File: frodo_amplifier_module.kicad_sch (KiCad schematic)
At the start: 24 parts, among them IC1 INA826AID, U1 NCS20071SN

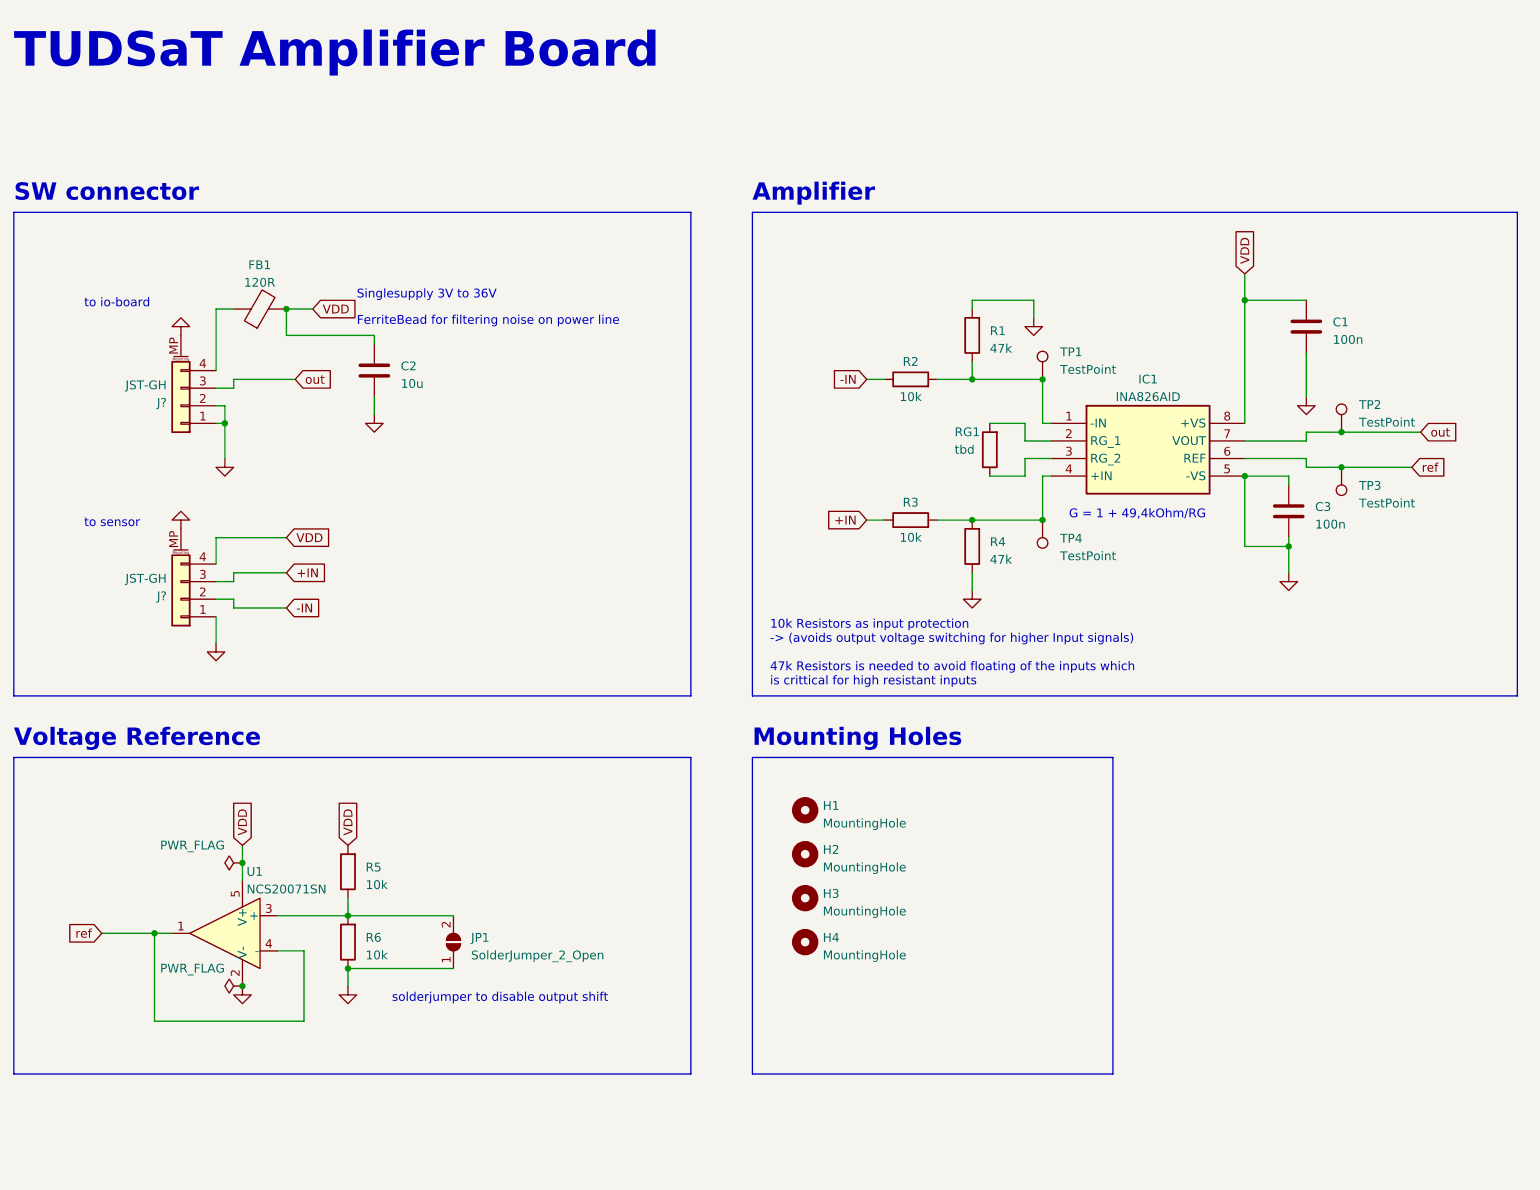
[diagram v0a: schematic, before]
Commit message: updated amplifier module, removed mounting holes and routed the pcb
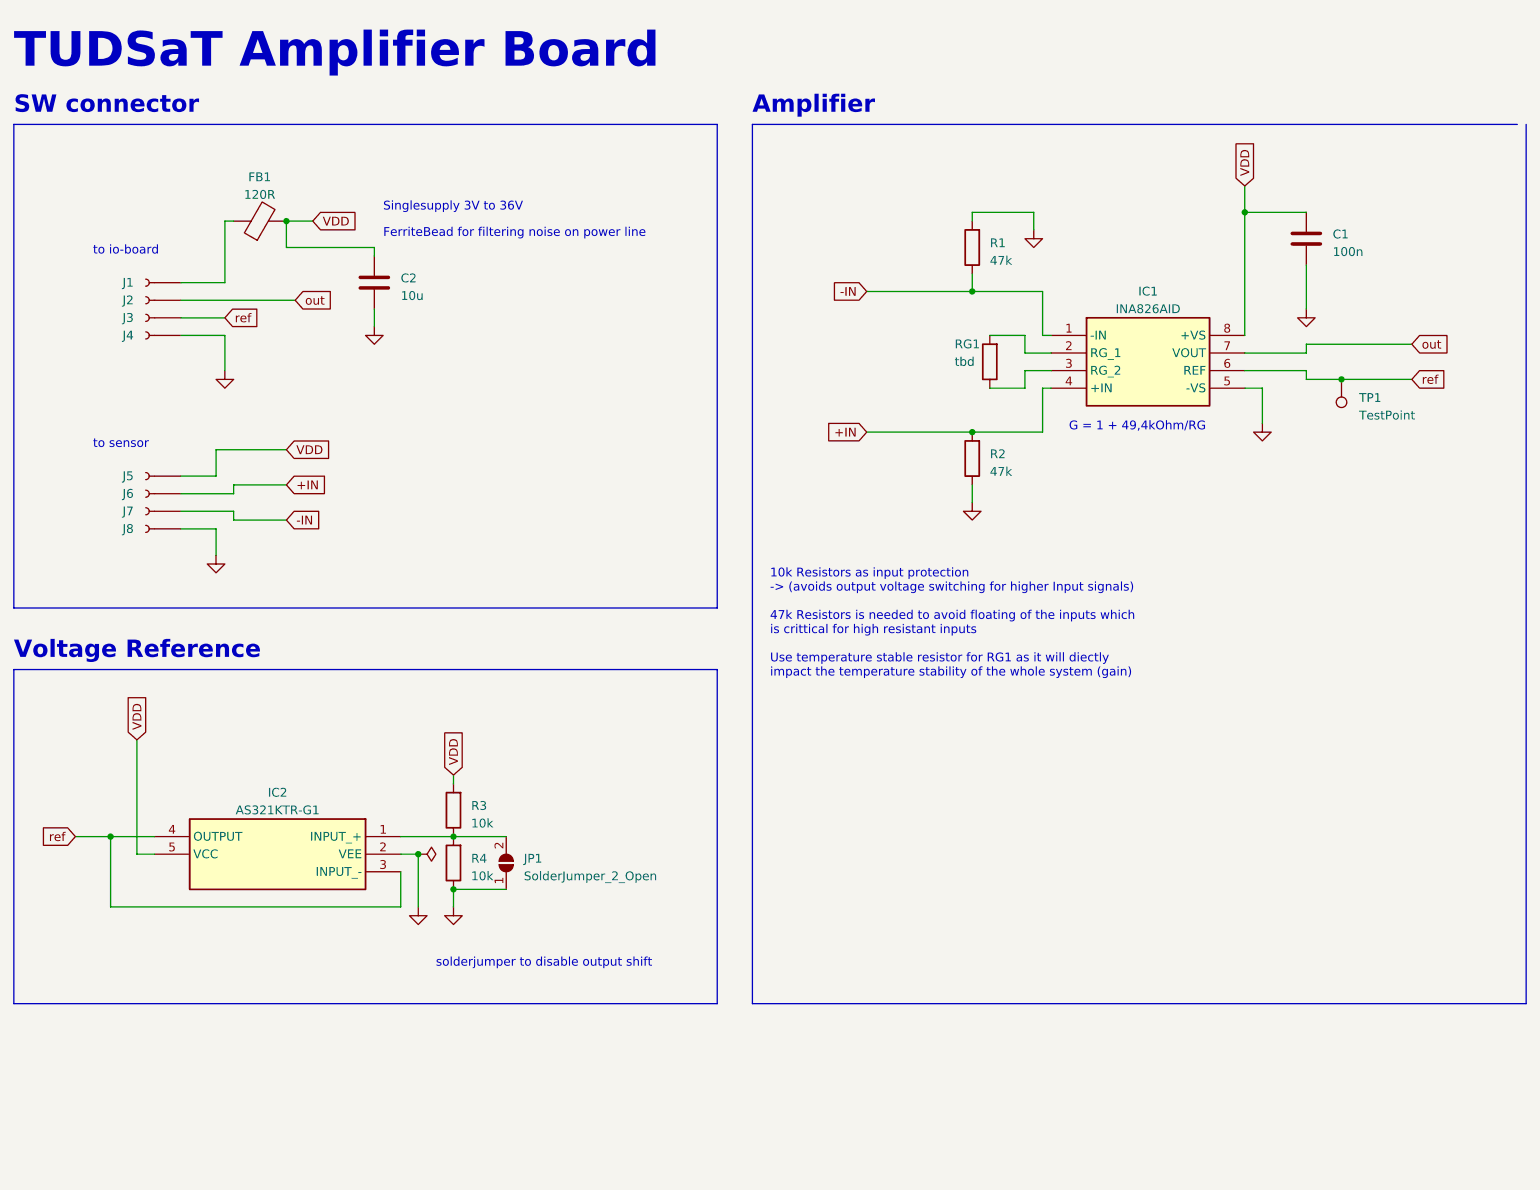
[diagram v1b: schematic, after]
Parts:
- removed C3: 100n, Capacitor_SMD:C_0402_1005Metric_Pad0.74x0.62mm_HandSolder, symbol Device:C
- removed H1, H2, H3, H4: MountingHole, MountingHole:MountingHole_2.2mm_M2_ISO7380_Pad, symbol Mechanical:MountingHole
- removed J? (x2): JST-GH, Connector_JST:JST_GH_SM04B-GHS-TB_1x04-1MP_P1.25mm_Horizontal, symbol Connector_Generic_MountingPin:Conn_01x04_MountingPin
- removed R2, R3: 10k, Resistor_SMD:R_0402_1005Metric_Pad0.72x0.64mm_HandSolder, symbol Device:R
- removed TP1, TP2, TP4: TestPoint, TestPoint:TestPoint_Pad_D1.5mm, symbol Connector:TestPoint
- removed U1: NCS20071SN, Package_SO:TSOP-5_1.65x3.05mm_P0.95mm, symbol Amplifier_Operational:NCS20071SN
- added IC2: AS321KTR-G1, Package_TO_SOT_SMD:SOT-23-5, symbol AS321KTR-G1:AS321KTR-G1
- added J1, J2, J3, J4, J5, J6, J7, J8: Conn_01x01_Socket, Connector_Wire:SolderWirePad_1x01_SMD_1x2mm, symbol Connector:Conn_01x01_Socket
- renumbered R4 to R2, R5 to R3, R6 to R4, TP3 to TP1
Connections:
- net +IN: now also IC1.4 (+IN), R2.2, J6.1 (Pin_1)
- net -IN: now also IC1.1 (-IN), R1.1, J7.1 (Pin_1)
- net GND: now also IC2.2 (VEE), J4.1 (Pin_1), J8.1 (Pin_1)
- net VDD: now also IC2.5 (VCC), J5.1 (Pin_1)
- net out: now also J2.1 (Pin_1)
- net ref: now also IC2.3 (INPUT_-), IC2.4 (OUTPUT), J3.1 (Pin_1)
- net at JP1.2 (B), R3.1, R4.2: now also IC2.1 (INPUT_+)
- net at FB1.1: now also J1.1 (Pin_1)
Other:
- note added: "10k Resistors as input protection -> (avoids output voltage switching for higher Input signals) 47k Resistors is needed to avoid floating of the inputs which is crittical for high resistant inputs Use temperature stable resistor for RG1 as it will diectly impact the temperature stability of the whole system (gain)"
- note removed: "10k Resistors as input protection -> (avoids output voltage switching for higher Input signals) 47k Resistors is needed to avoid floating of the inputs which is crittical for high resistant inputs"
- note removed: "Mounting Holes"
- moved on the sheet: C1, C2, FB1, IC1, JP1, R1, R2, R3, R4, RG1, TP1

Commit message: updated stuff
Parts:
- removed JP1: SolderJumper_2_Open, Jumper:SolderJumper-2_P1.3mm_Open_Pad1.0x1.5mm, symbol Jumper:SolderJumper_2_Open
- removed TP1: TestPoint, TestPoint:TestPoint_Pad_D1.5mm, symbol Connector:TestPoint
- added JP1: SolderJumper_3_Open, Jumper:SolderJumper-3_P1.3mm_Open_RoundedPad1.0x1.5mm_NumberLabels, symbol Jumper:SolderJumper_3_Open
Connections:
- net GND: now also JP1.1 (A)
- net at R3.1, R4.2: now also JP1.3 (B); no longer IC2.1 (INPUT_+)
- new net: IC2.1 (INPUT_+), JP1.2 (C)
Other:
- moved on the sheet: R3, R4

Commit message: added stuff
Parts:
- added H1, H2: MountingHole, MountingHole:MountingHole_3.2mm_M3, symbol Mechanical:MountingHole
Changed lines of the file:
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@@
+    )
+  )
+  (symbol (lib_id "Mechanical:MountingHole") (at 39.37 171.45 0) (unit 1)
+    (in_bom yes) (on_board yes) (dnp no) (fields_autoplaced)
+    (property "Reference" "H1" (at 41.91 170.815 0)
+      (effects (font (size 1.27 1.27)) (justify left))
+    )
+    (property "Value" "MountingHole" (at 41.91 173.355 0)
+      (effects (font (size 1.27 1.27)) (justify left))
+    )
+    (property "Footprint" "MountingHole:MountingHole_3.2mm_M3" (at 39.37 171.45 0)
+      (effects (font (size 1.27 1.27)) hide)
+    )
+    (property "Datasheet" "~" (at 39.37 171.45 0)
+      (effects (font (size 1.27 1.27)) hide)
+    )
+    (instances
+      (project "frodo_amplifier_module"
+        (path "/61190ca3-2171-4daf-b151-7360302be40b"
+          (reference "H1") (unit 1)
+        )
+      )
     )
   )
@@
         )
       )
+    )
+  )
+  (symbol (lib_id "Mechanical:MountingHole") (at 39.37 177.8 0) (unit 1)
+    (in_bom yes) (on_board yes) (dnp no) (fields_autoplaced)
+    (property "Reference" "H2" (at 41.91 177.165 0)
+      (effects (font (size 1.27 1.27)) (justify left))
+    )
+    (property "Value" "MountingHole" (at 41.91 179.705 0)
+      (effects (font (size 1.27 1.27)) (justify left))
+    )
+    (property "Footprint" "MountingHole:MountingHole_3.2mm_M3" (at 39.37 177.8 0)
+      (effects (font (size 1.27 1.27)) hide)
+    )
+    (property "Datasheet" "~" (at 39.37 177.8 0)
+      (effects (font (size 1.27 1.27)) hide)
+    )
+    (instances
+      (project "frodo_amplifier_module"
+        (path "/61190ca3-2171-4daf-b151-7360302be40b"
+          (reference "H2") (unit 1)
+        )
+      )

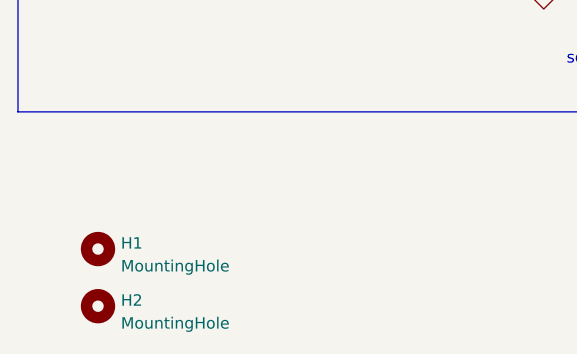
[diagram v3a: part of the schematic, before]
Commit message: fixed soulder jumper, added mousbites
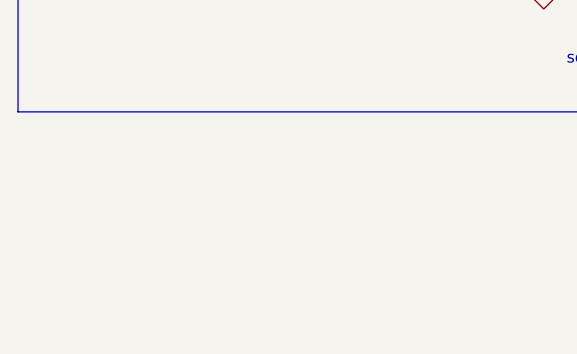
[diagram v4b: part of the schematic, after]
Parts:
- removed H1, H2: MountingHole, MountingHole:MountingHole_3.2mm_M3, symbol Mechanical:MountingHole
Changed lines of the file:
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@@
-    )
-  )
-  (symbol (lib_id "Mechanical:MountingHole") (at 39.37 171.45 0) (unit 1)
-    (in_bom yes) (on_board yes) (dnp no) (fields_autoplaced)
-    (property "Reference" "H1" (at 41.91 170.815 0)
-      (effects (font (size 1.27 1.27)) (justify left))
-    )
-    (property "Value" "MountingHole" (at 41.91 173.355 0)
-      (effects (font (size 1.27 1.27)) (justify left))
-    )
-    (property "Footprint" "MountingHole:MountingHole_3.2mm_M3" (at 39.37 171.45 0)
-      (effects (font (size 1.27 1.27)) hide)
-    )
-    (property "Datasheet" "~" (at 39.37 171.45 0)
-      (effects (font (size 1.27 1.27)) hide)
-    )
-    (instances
-      (project "frodo_amplifier_module"
-        (path "/61190ca3-2171-4daf-b151-7360302be40b"
-          (reference "H1") (unit 1)
-        )
-      )
     )
   )
@@
         )
       )
-    )
-  )
-  (symbol (lib_id "Mechanical:MountingHole") (at 39.37 177.8 0) (unit 1)
-    (in_bom yes) (on_board yes) (dnp no) (fields_autoplaced)
-    (property "Reference" "H2" (at 41.91 177.165 0)
-      (effects (font (size 1.27 1.27)) (justify left))
-    )
-    (property "Value" "MountingHole" (at 41.91 179.705 0)
-      (effects (font (size 1.27 1.27)) (justify left))
-    )
-    (property "Footprint" "MountingHole:MountingHole_3.2mm_M3" (at 39.37 177.8 0)
-      (effects (font (size 1.27 1.27)) hide)
-    )
-    (property "Datasheet" "~" (at 39.37 177.8 0)
-      (effects (font (size 1.27 1.27)) hide)
-    )
-    (instances
-      (project "frodo_amplifier_module"
-        (path "/61190ca3-2171-4daf-b151-7360302be40b"
-          (reference "H2") (unit 1)
-        )
-      )
